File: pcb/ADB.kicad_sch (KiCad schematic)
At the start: 54 parts, among them J1 Conn_01x10_Socket, J10 Conn_02x02_Counter_Clockwise, J11 Conn_02x02_Counter_Clockwise, J12 Conn_02x02_Counter_Clockwise, J13 Conn_02x02_Counter_Clockwise, J14 Conn_01x02_Socket, J15 Conn_01x04_Socket, J16 Conn_01x02_Socket, J17 Conn_01x02_Socket, J18 Conn_01x02_Socket, J19 Conn_01x03_Socket, J2 Conn_01x03_Pin, J20 Conn_01x03_Socket, J21 Conn_01x02_Socket, J22 Conn_01x02_Socket, J23 Conn_01x04_Socket, J24 Conn_01x02_Socket, J25 Conn_01x02_Socket, J26 Conn_01x02_Socket, J27 Conn_01x02_Socket, J28 Conn_01x02_Socket, J29 Conn_01x02_Socket, J3 Conn_01x08_Pin, J30 Conn_01x04_Socket, J31 Conn_01x02_Socket, J32 Conn_01x02_Socket, J33 Conn_01x02_Socket, J34 Conn_01x03_Socket, J35 Conn_01x03_Socket, J36 Conn_01x02_Socket, J37 Conn_01x02_Socket, J38 Conn_01x04_Socket, J39 Conn_01x02_Socket, J4 Conn_01x02_Pin, J40 Conn_01x02_Socket, J41 Conn_01x02_Socket, J42 Conn_01x02_Socket, J43 Conn_01x02_Socket, J5 Conn_01x10_Socket, J6 Conn_02x02_Counter_Clockwise, J7 Conn_02x02_Counter_Clockwise, J8 Conn_02x02_Counter_Clockwise, J9 Conn_02x02_Counter_Clockwise, U1 LM358

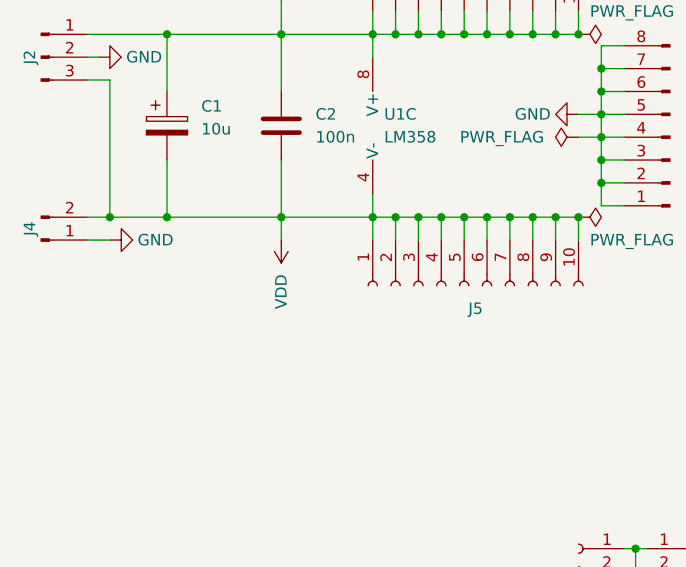
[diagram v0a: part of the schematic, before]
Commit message: Fix negative voltage descriptors
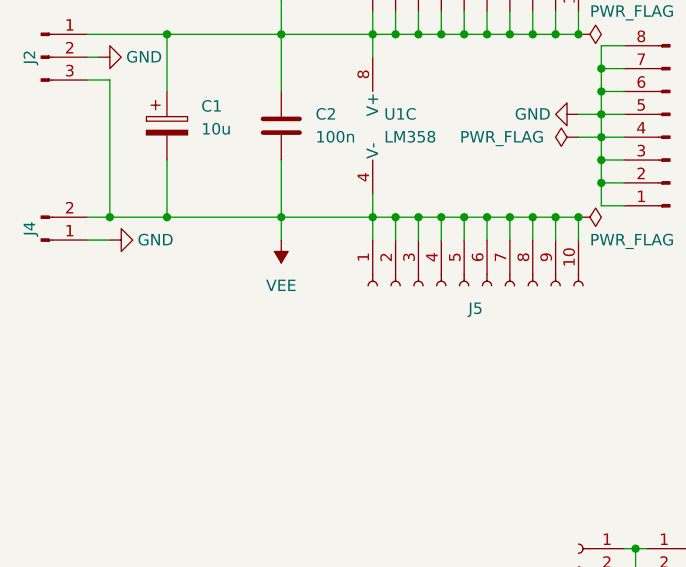
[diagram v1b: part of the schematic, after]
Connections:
- net VDD renamed VEE
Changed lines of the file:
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@@
-    )
-  )
-  (symbol (lib_id "power:VDD") (at 55.88 50.8 180) (unit 1)
-    (in_bom yes) (on_board yes) (dnp no) (fields_autoplaced)
-    (property "Reference" "#PWR05" (at 55.88 46.99 0)
-      (effects (font (size 1.27 1.27)) hide)
-    )
-    (property "Value" "VDD" (at 55.88 54.61 90)
-      (effects (font (size 1.27 1.27)) (justify left))
-    )
-    (property "Footprint" "" (at 55.88 50.8 0)
-      (effects (font (size 1.27 1.27)) hide)
-    )
-    (property "Datasheet" "" (at 55.88 50.8 0)
-      (effects (font (size 1.27 1.27)) hide)
-    )
-    (pin "1")
-    (instances
-      (project "ADB"
-        (path "/9334361a-f7a5-4302-90e9-4b89798c8fc6"
-          (reference "#PWR05") (unit 1)
-        )
-      )
     )
   )
@@
         )
       )
+    )
+  )
+  (symbol (lib_id "power:VEE") (at 55.88 50.8 180) (unit 1)
+    (in_bom yes) (on_board yes) (dnp no) (fields_autoplaced)
+    (property "Reference" "#PWR05" (at 55.88 46.99 0)
+      (effects (font (size 1.27 1.27)) hide)
+    )
+    (property "Value" "VEE" (at 55.88 55.88 0)
+      (effects (font (size 1.27 1.27)))
+    )
+    (property "Footprint" "" (at 55.88 50.8 0)
+      (effects (font (size 1.27 1.27)) hide)
+    )
+    (property "Datasheet" "" (at 55.88 50.8 0)
+      (effects (font (size 1.27 1.27)) hide)
+    )
+    (pin "1")
+    (instances
+      (project "ADB"
+        (path "/9334361a-f7a5-4302-90e9-4b89798c8fc6"
+          (reference "#PWR05") (unit 1)
+        )
+      )

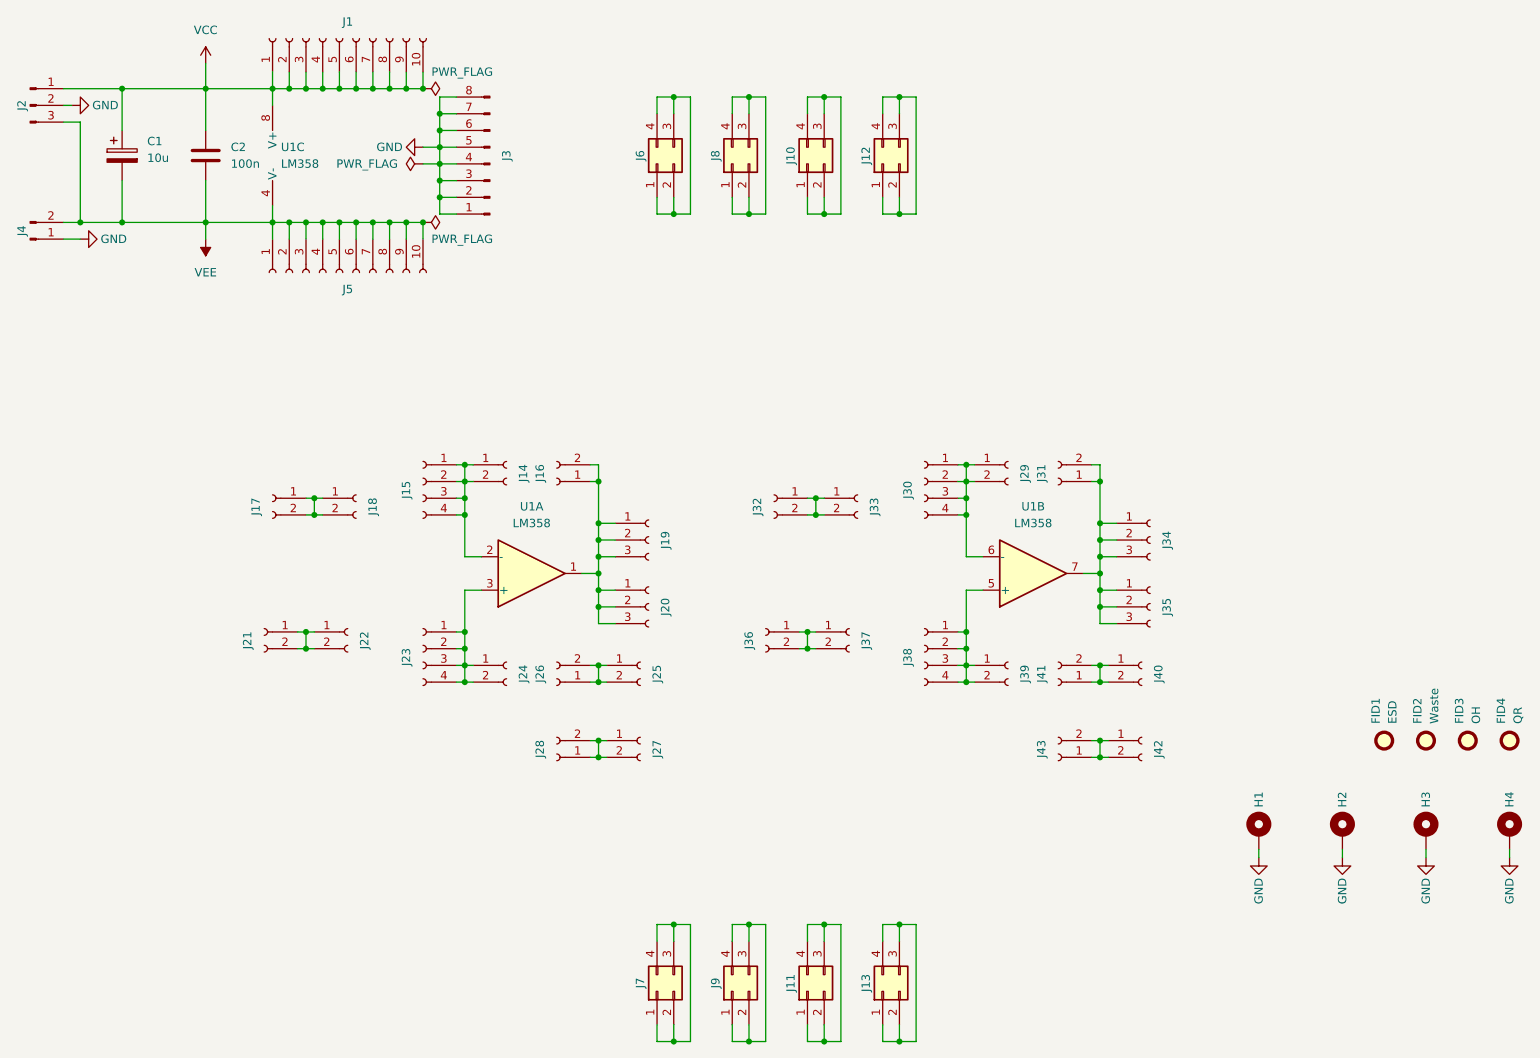
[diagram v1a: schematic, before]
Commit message: Add reverse polarity protection
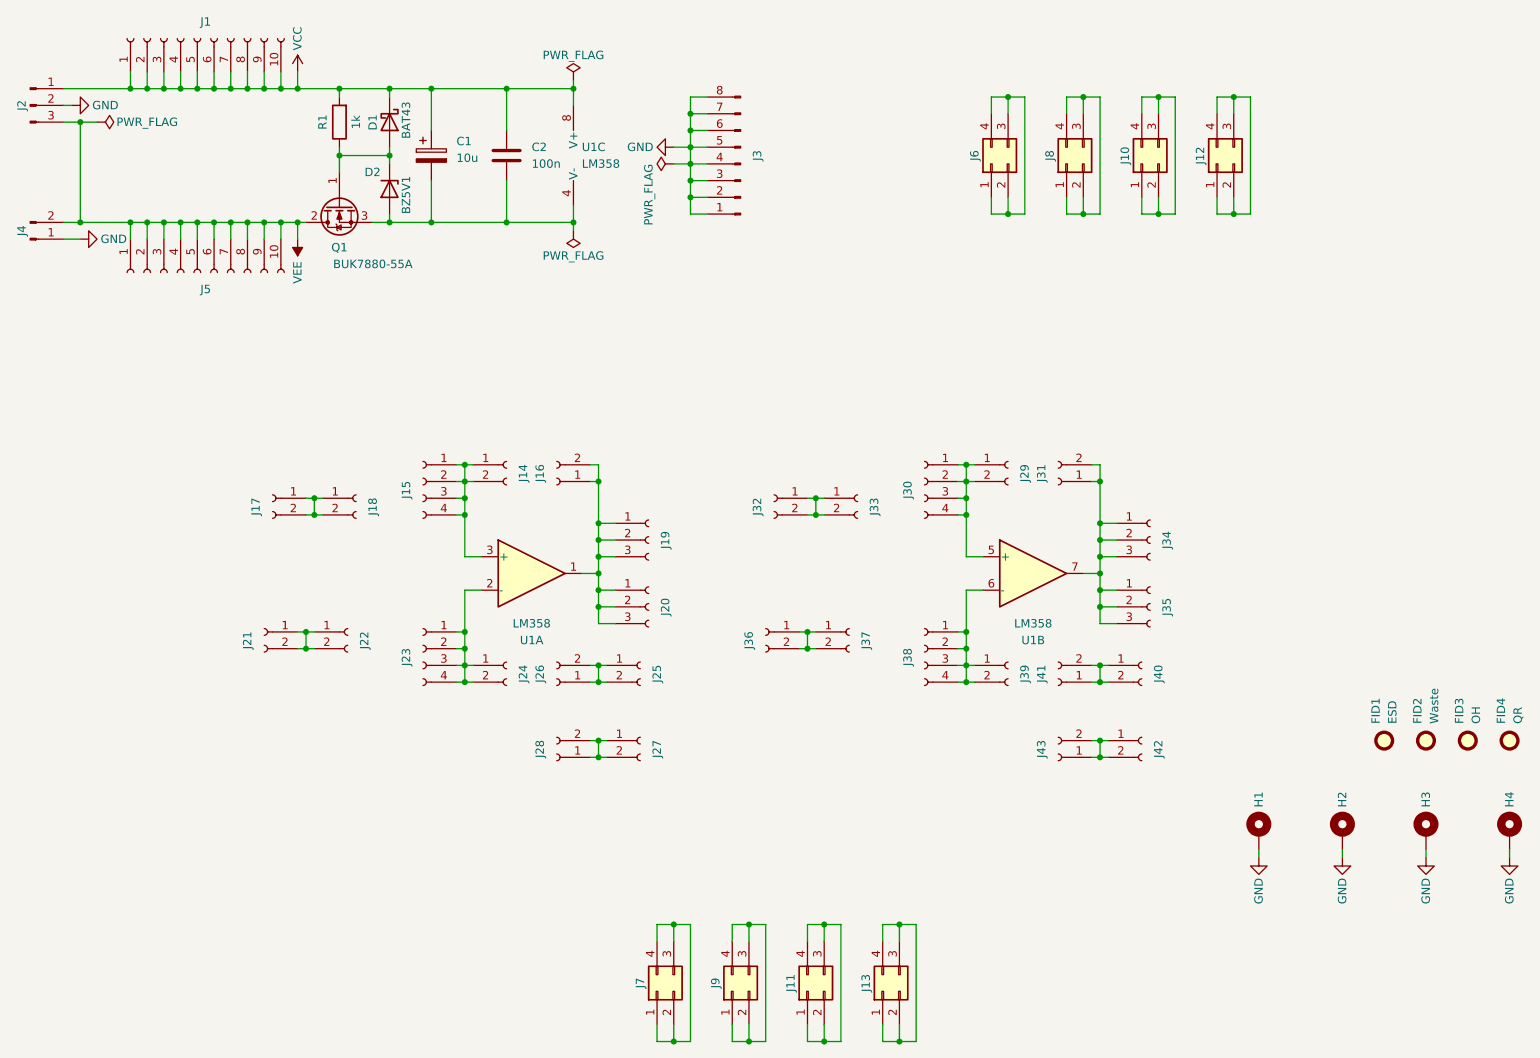
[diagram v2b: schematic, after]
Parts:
- added D1: BAT43, Diode_SMD:D_MiniMELF, symbol Device:D_Schottky
- added D2: BZ5V1, Diode_SMD:D_MiniMELF, symbol Diode:BZV55B15
- added Q1: BUK7880-55A, Package_TO_SOT_SMD:SOT-223-3_TabPin2, symbol Transistor_FET:BUK7880-55A
- added R1: 1k, Resistor_SMD:R_1206_3216Metric, symbol Device:R
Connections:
- net VCC: now also D1.1 (K), R1.2
- net VEE: now also Q1.2 (D); no longer C1.2, C2.2, U1.4 (V-)
- net at J38.1 (Pin_1), J38.2 (Pin_2), J38.3 (Pin_3)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: now also U1.6 (-); no longer U1.5 (+)
- net at J29.1 (Pin_1), J29.2 (Pin_2), J30.1 (Pin_1)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: now also U1.5 (+); no longer U1.6 (-)
- net at J23.1 (Pin_1), J23.2 (Pin_2), J23.3 (Pin_3)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: now also U1.2 (-); no longer U1.3 (+)
- net at J14.1 (Pin_1), J14.2 (Pin_2), J15.1 (Pin_1)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: now also U1.3 (+); no longer U1.2 (-)
- new net: D1.2 (A), D2.1 (K), Q1.1 (G), R1.1
- new net: C1.2, C2.2, D2.2 (A), Q1.3 (S), U1.4 (V-)
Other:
- moved on the sheet: C1, C2, J1, J10, J12, J3, J5, J6, J8, U1C
